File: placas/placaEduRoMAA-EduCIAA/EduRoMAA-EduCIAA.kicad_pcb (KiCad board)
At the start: 2 copper layers, 103 x 80 mm, 81 parts, among them J1 DC_IN, J2 Motor_Izq, J3 Motor_Der, J4 Bluetooth, J5 Sonar, J6 DC_OUT, J7 DC_IN, Q1 BC548, Q2 BC548, Q3 BC548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

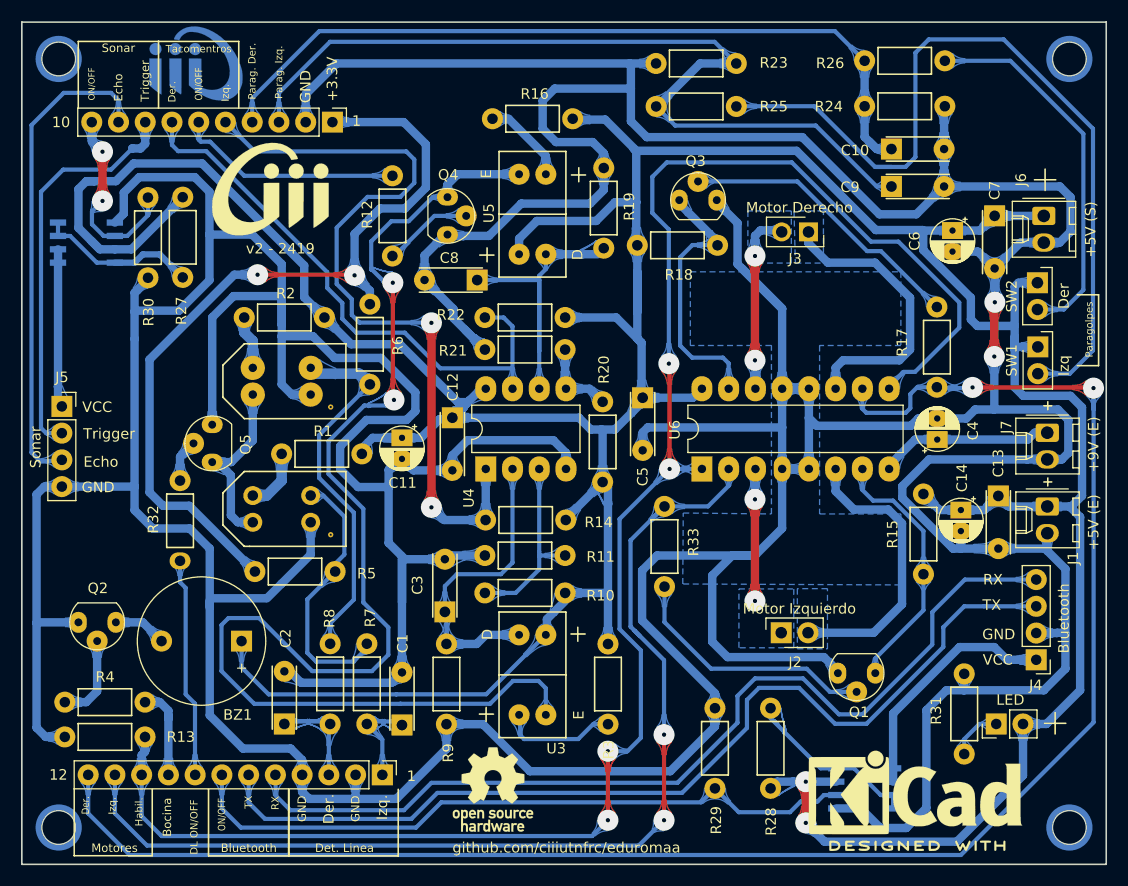
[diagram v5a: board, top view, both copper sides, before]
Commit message: [PCB] Agrego nombre de placa y reorganizo pistas.
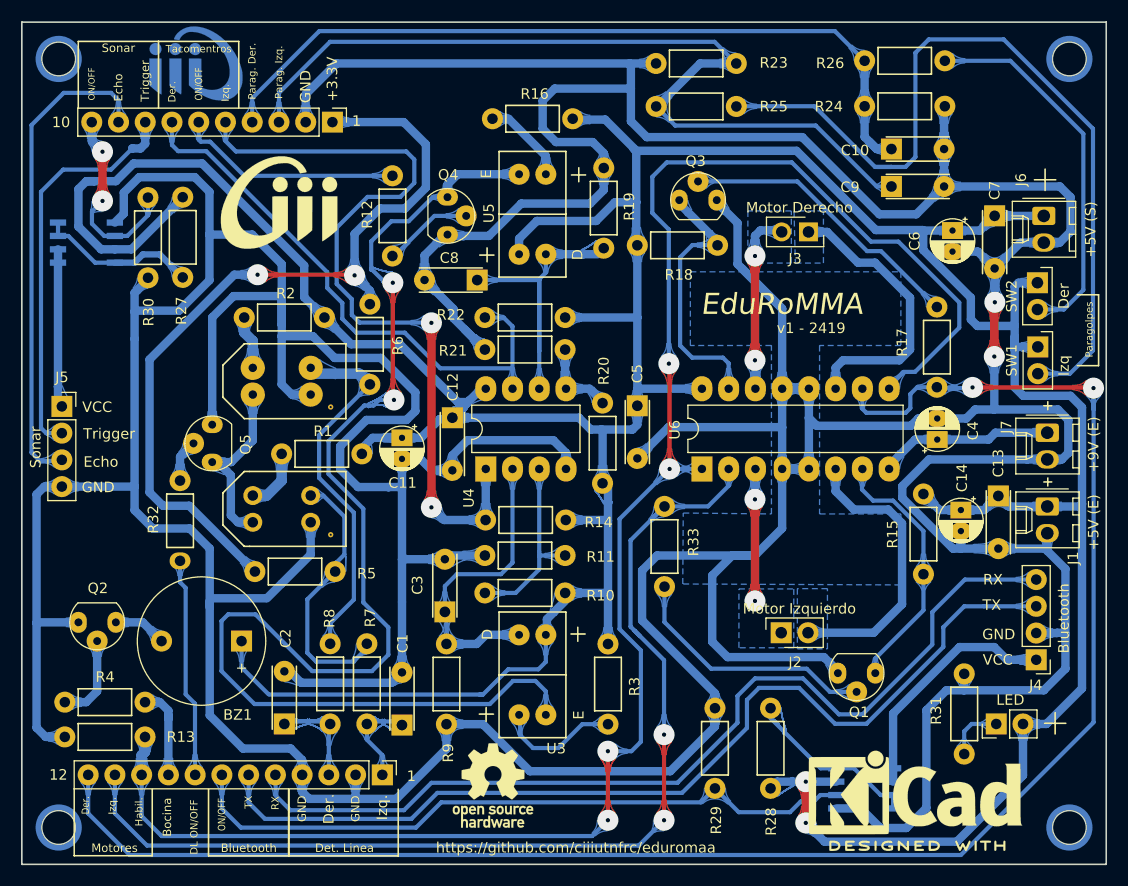
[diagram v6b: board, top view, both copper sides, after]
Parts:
- moved Logo_2 1.51 mm to (90.4, 72.1)
- moved C5 0.92 mm to (124.5, 91.4)
- moved Logo_3 0.38 mm to (110.7, 127.5)
- moved R20 0.12 mm to (121.2, 98.8)
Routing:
- net +5V: track 406.4 -> 401.3 mm
- net GND: track 756.9 -> 753.3 mm
- net Encoder_Izq: track 75.5 -> 76.6 mm
- net Net-(R3-Pad2): track 10.4 -> 11.1 mm
- net /Motor_Der1: track 27.6 -> 27.0 mm
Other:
- board text added: "EduRoMMA"
- board text added: "https://github.com/ciiiutnfrc/eduromaa"
- board text added: "v1 - 2419"
- board text removed: "github.com/ciiiutnfrc/eduromaa"
- board text removed: "v2 - 2419"
